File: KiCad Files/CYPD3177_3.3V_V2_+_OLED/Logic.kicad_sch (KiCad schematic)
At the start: 33 parts, among them J5 0.91 OLED, J6 QWIIC, J7 Conn_01x05, J8 I2C_3.3V, Q1 DMC2990UDJ-7, SW1 GT-TC0060-H050-L1, SW2 B3U-1000P, U1 TCA9406DC, U2 INA238, U9 ATtiny3217-M

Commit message: changes
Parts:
- added D6: PMEG6020ER, Diode_SMD:D_SOD-123F, symbol Diode:PMEG6020ER
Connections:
- net GND: now also D6.2 (A)
- net LOGIC_SW: now also U9.22 (PC5); no longer U9.1 (PA2)
- net PGOOD: now also U9.2 (PA3); no longer U9.22 (PC5)
- net Rail_2: now also D6.1 (K)
- net SW_LEFT: now also U9.1 (PA2); no longer U9.2 (PA3)
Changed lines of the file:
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@@
 	)
 	(junction
+		(at 78.74 179.07)
+		(diameter 0)
+		(color 0 0 0 0)
+	)
+	(junction
+		(at 78.74 185.42)
+		(diameter 0)
+		(color 0 0 0 0)
+	)
+	(junction
 		(at 158.75 87.63)
 		(diameter 0)
@@
 	(wire
 		(pts
+			(xy 78.74 185.42) (xy 78.74 187.96)
+		)
+		(stroke
+			(width 0)
+			(type default)
+		)
+	)
+	(wire
+		(pts
 			(xy 78.74 168.91) (xy 82.55 168.91)
 		)
@@
 	(wire
 		(pts
+			(xy 156.21 93.98) (xy 156.21 92.71)
+		)
+		(stroke
+			(width 0)
+			(type default)
+		)
+	)
+	(wire
+		(pts
 			(xy 175.26 110.49) (xy 156.21 110.49)
 		)
@@
 	(wire
 		(pts
+			(xy 82.55 185.42) (xy 78.74 185.42)
+		)
+		(stroke
+			(width 0)
+			(type default)
+		)
+	)
+	(wire
+		(pts
+			(xy 78.74 179.07) (xy 78.74 185.42)
+		)
+		(stroke
+			(width 0)
+			(type default)
+		)
+	)
+	(wire
+		(pts
 			(xy 78.74 179.07) (xy 82.55 179.07)
 		)
@@
 			"AAAAAAAAAAAAAAAAAAAAAAAAAAAAAAAAAAAAAAAAAAAAAAAAAAAAAAAAAAAAAAAAAAAAAAAAAAAA"
 			"AAAAAAAAAAAAAAAAAAAAAAAAAAAAAAAAAAAAAAAAAAAAAAAAAAAAAAAAAAAAAAAAAAAAAAAAAAAA"
+			"AAAAAAAAAAAAAAAAAAAAAAAAAAAAAAAAAAAAAAAAAAAAAAAAAAAAAAAAAAAAAAAAAAAAAAAAAAAA"
+			"AAAAAAAAAAAAAAAAAAAAAAAAAAAAAAAAAAAAAAAAAAAAAAAAAAAAAAAAAAAAAAAAAAAAAAAAAAAA"
+			"AAAAAAAAAAAAAAAAAAAAAAAAAAAAAAAAAAAAAAAAAAAAAAAAAAAAAAAAAAAAAAAAAAAAAAAAAAAA"
+			"AAAAAAAAAAAAAAAAAAAAAAAAAAAAAAAAAAAAAAAAAAAAAAAAAAAAAAAAAAAAAAAAAAAAAAAAAAAA"
+			"AAAAAAAAAAAAAAAAAAAAAAAAAAAAAAAAAAAAAAAAAAAAAAAAAAAAAAAAAAAAAAAAAAAAAAAAAAAA"
+			"AAAAAAAAAAAAAAAAAAAAAAAAAAAAAAAAAAAAAAAAAAAAAAAAAAAAAAAAAAAAAAAAAAAAAAAAAAAA"
+			"AAAAAAAAAAAAAAAAAAAAAAAAAAAAAAAAAAAAAAAAAAAAAAAAAAAAAAAAAAAAAAAAAAAAAAAAAAAA"
+			"AAAAAAAAAAAAAAAAAAAAAAAAAAAAAAAAAAAAAAAAAAAAAAAAAAAAAAAAAAAAAAAAAAAAAAAAAAAA"
+			"AAAAAAAAAAAAAAAAAAAAAAAAAAAAAAAAAAAAAAAAAAAAAAAAAAAAAAAAAAAAAAAAAAAAAAAAAAAA"
+			"AAAAAAAAAAAAAAAAAAAAAAAAAAAAAAAAAAAAAAAAAAAAAAAAAAAAAAAAAAAAAAAAAAAAAAAAAAAA"
+			"AAAAAAAAAAAAAAAAAAAAAAAAAAAAAAAAAAAAAAAAAAAAAAAAAAAAAAAAAAAAAAAAAAAAAAAAAAAA"
+			"AAAAAAAAAAAAAAAAAAAAAAAAAAAAAAAAAAAAAAAAAAAAAAAAAAAAAAAAAAAAAAAAAAAAAAAAAAAA"
+			"AAAAAAAAAAAAAAAAAAAAAAAAAAAAAAAAAAAAAAAAAAAAAAAAAAAAAAAAAAAAAAAAAAAAAAAAAAAA"
+			"AAAAAAAAAAAAAAAAAAAAAAAAAAAAAAAAAAAAAAAAAAAAAAAAAAAAAAAAAAAAAAAAAAAAAAAAAAAA"
+			"AAAAAAAAAAAAAAAAAAAAAAAAAAAAAAAAAAAAAAAAAAAAAAAAAAAAAAAAAAAAAAAAAAAAAAAAAAAA"
+			"AAAAAAAAAAAAAAAAAAAAAAAAAAAAAAAAAAAAAAAAAAAAAAAAAAAAAAAAAAAAAAAAAAAAAAAAAAAA"
+			"AAAAAAAAAAAAAAAAAAAAAAAAAAAAAAAAAAAAAAAAAAAAAAAAAAAAAAAAAAAAAAAAAAAAAAAAAAAA"
+			"AAAAAAAAAAAAAAAAAAAAAAAAAAAAAAAAAAAAAAAAAAAAAAAAAAAAAAAAAAAAAAAAAAAAAAAAAAAA"
 			"AAAAAAAAAAAAAAAAAAAAAAAAAAAAAAAAAAAAAAAAAAAAAAAAAA=="
 		)
@@
 	)
 	(label "SW_LEFT"
-		(at 161.29 95.25 0)
+		(at 156.21 93.98 0)
 		(effects
 			(font
@@
 		)
 	)
+	(hierarchical_label "LOGIC_SW"
+		(shape input)
+		(at 125.73 123.19 180)
+		(effects
+			(font
+				(size 1.27 1.27)
+			)
+			(justify right)
+		)
+	)
 	(hierarchical_label "SDA"
 		(shape bidirectional)
@@
 	(hierarchical_label "Rail_2"
 		(shape output)
-		(at 78.74 179.07 270)
+		(at 78.74 187.96 270)
 		(effects
 			(font
@@
 	(hierarchical_label "PGOOD"
 		(shape output)
-		(at 125.73 123.19 180)
+		(at 161.29 95.25 0)
 		(effects
 			(font
 				(size 1.27 1.27)
 			)
-			(justify right)
+			(justify left)
 		)
 	)
@@
 		)
 	)
-	(hierarchical_label "LOGIC_SW"
-		(shape input)
-		(at 156.21 92.71 0)
-		(effects
-			(font
-				(size 1.27 1.27)
-			)
-			(justify left)
-		)
-	)
 	(hierarchical_label "SDA_3.3v"
 		(shape bidirectional)
@@
 	)
 	(symbol
+		(lib_id "Diode:PMEG6020ER")
+		(at 86.36 185.42 0)
+		(unit 1)
+		(exclude_from_sim no)
+		(in_bom yes)
+		(on_board yes)
+		(dnp no)
+		(property "Reference" "D6"
+			(at 83.566 192.278 90)
+			(effects
+				(font
+					(size 1.27 1.27)
+				)
+				(justify left)
+			)
+		)
+		(property "Value" "PMEG6020ER"
+			(at 90.678 196.596 90)
+			(effects
+				(font
+					(size 1.27 1.27)
+				)
+				(justify left)
+			)
+		)
+		(property "Footprint" "Diode_SMD:D_SOD-123F"
+			(at 86.36 189.865 0)
+			(effects
+				(font
+					(size 1.27 1.27)
+				)
+				(hide yes)
+			)
+		)
+		(property "Datasheet" "https://assets.nexperia.com/documents/data-sheet/PMEG6020ER.pdf"
+			(at 86.36 185.42 0)
+			(effects
+				(font
+					(size 1.27 1.27)
+				)
+				(hide yes)
+			)
+		)
+		(property "Description" "60V, 2A low Vf MEGA Schottky barrier rectifier, SOD-123W"
+			(at 86.36 185.42 0)
+			(effects
+				(font
+					(size 1.27 1.27)
+				)
+				(hide yes)
+			)
+		)
+		(pin "1"
+		)
+		(pin "2"
+		)
+		(instances
+			(project "CYPD3177_3.3V_V2_+_OLED"
+				(path "/a370047b-ebc6-4236-825e-9462ba7e4392/bd19bb82-a076-4c57-9538-864609224ca0"
+					(reference "D6")
+					(unit 1)
+				)
+			)
+		)
+	)
+	(symbol
 		(lib_id "power:GND")
 		(at 90.17 154.94 270)
@@
 					(unit 1)
 				)
+			)
+		)
+	)
+	(symbol
+		(lib_id "power:GND")
+		(at 90.17 185.42 90)
+		(unit 1)
+		(exclude_from_sim no)
+		(in_bom yes)
+		(on_board yes)
+		(dnp no)
+		(fields_autoplaced yes)
+		(property "Reference" "#PWR056"
+			(at 96.52 185.42 0)
+			(effects
+				(font
+					(size 1.27 1.27)
+				)
+				(hide yes)
+			)
+		)
+		(property "Value" "GND"
+			(at 95.25 185.42 0)
+			(effects
+				(font
+					(size 1.27 1.27)
+				)
+				(hide yes)
+			)
+		)
+		(property "Footprint" ""
+			(at 90.17 185.42 0)
+			(effects
+				(font
+					(size 1.27 1.27)
+				)
+				(hide yes)
+			)
+		)
+		(property "Datasheet" ""
+			(at 90.17 185.42 0)
+			(effects
+				(font
+					(size 1.27 1.27)
+				)
+				(hide yes)
+			)
+		)
+		(property "Description" ""
+			(at 90.17 185.42 0)
+			(effects
+				(font
+					(size 1.27 1.27)
+				)
+				(hide yes)
+			)
+		)
+		(pin "1"
+		)
+		(instances
+			(project "CYPD3177_3.3V_V2_+_OLED"
+				(path "/a370047b-ebc6-4236-825e-9462ba7e4392/bd19bb82-a076-4c57-9538-864609224ca0"
+					(reference "#PWR056")
+					(unit 1)
+				)

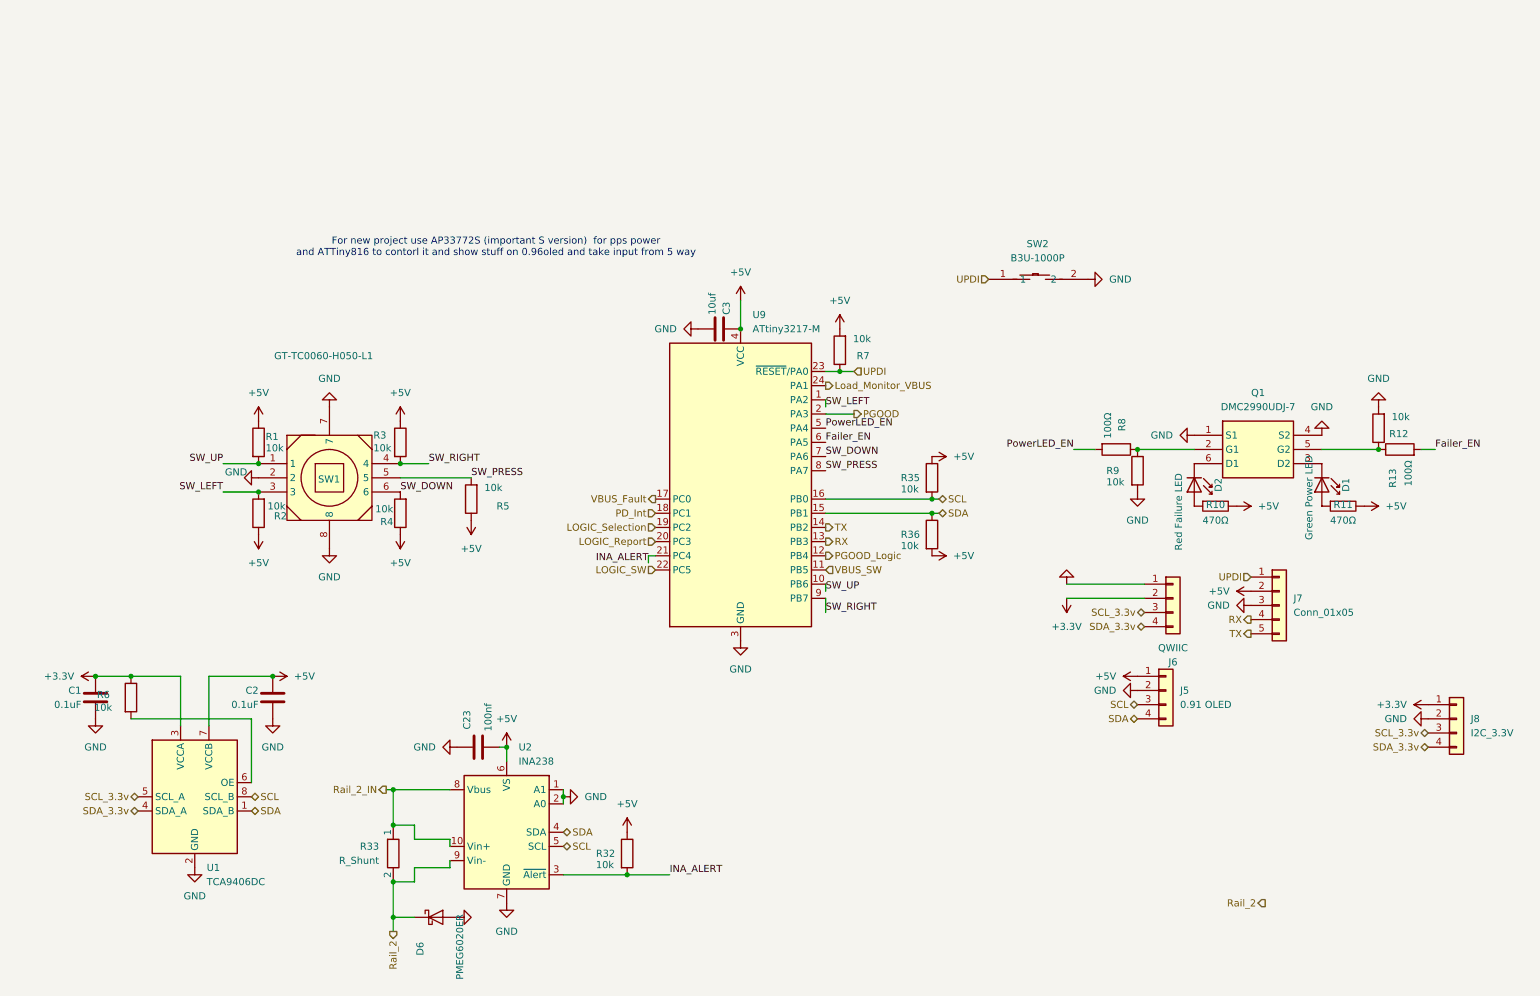
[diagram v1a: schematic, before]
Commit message: CYPD3177 wiring finshed, only silkscreen needs changes and make a breakout board
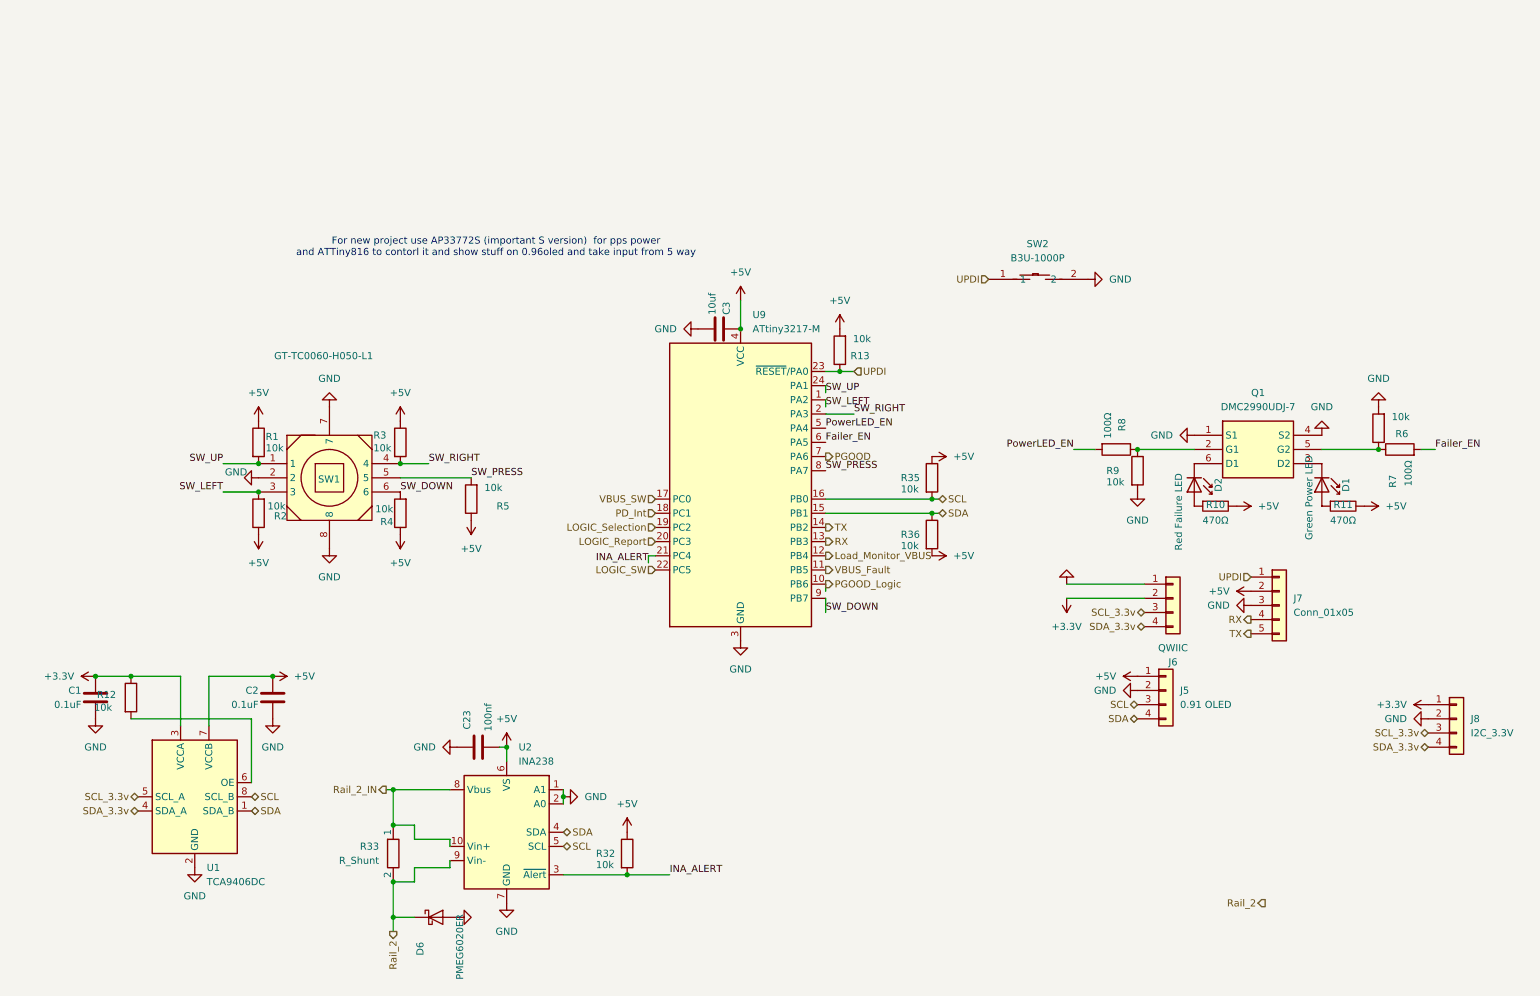
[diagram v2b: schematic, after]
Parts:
- R10, R11: footprint Resistor_SMD:R_0402_1005Metric_Pad0.72x0.64mm_HandSolder -> Resistor_SMD:R_0402_1005Metric
- renumbered R6 to R12, R7 to R13, R12 to R6, R13 to R7
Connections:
- net Load_Monitor_VBUS: now also U9.12 (PB4); no longer U9.24 (PA1)
- net PGOOD: now also U9.7 (PA6); no longer U9.2 (PA3)
- net PGOOD_Logic: now also U9.10 (PB6); no longer U9.12 (PB4)
- net SW_DOWN: now also U9.9 (PB7); no longer U9.7 (PA6)
- net SW_RIGHT: now also U9.2 (PA3); no longer U9.9 (PB7)
- net SW_UP: now also U9.24 (PA1); no longer U9.10 (PB6)
- net VBUS_Fault: now also U9.11 (PB5); no longer U9.17 (PC0)
- net VBUS_SW: now also U9.17 (PC0); no longer U9.11 (PB5)
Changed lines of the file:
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@@
 	(wire
 		(pts
+			(xy 156.21 91.44) (xy 156.21 90.17)
+		)
+		(stroke
+			(width 0)
+			(type default)
+		)
+	)
+	(wire
+		(pts
 			(xy 156.21 127) (xy 156.21 125.73)
 		)
@@
 			"AAAAAAAAAAAAAAAAAAAAAAAAAAAAAAAAAAAAAAAAAAAAAAAAAAAAAAAAAAAAAAAAAAAAAAAAAAAA"
 			"AAAAAAAAAAAAAAAAAAAAAAAAAAAAAAAAAAAAAAAAAAAAAAAAAAAAAAAAAAAAAAAAAAAAAAAAAAAA"
-			"AAAAAAAAAAAAAAAAAAAAAAAAAAAAAAAAAAAAAAAAAAAAAAAAAA=="
-		)
-	)
-	(label "SW_DOWN"
-		(at 156.21 102.87 0)
-		(effects
-			(font
-				(size 1.27 1.27)
-			)
-			(justify left bottom)
+			"AAAAAAAAAAAAAAAAAAAAAAAAAAAAAAAAAAAAAAAAAAAAAAAAAAAAAAAAAAAAAAAAAAAAAAAAAAAA"
+			"AAAAAAAAAAAAAAAAAAAAAAAAAAAAAAAAAAAAAAAAAAAAAAAAAAAAAAAAAAAAAAAAAAAAAAAAAAAA"
+			"AAAAAAAAAAAAAAAAAAAAAAAAAAAAAAAAAAAAAAAAAAAAAAAAAAAAAAAAAAAAAAAAAAAAAAAAAAAA"
+			"AAAAAAAAAAAAAAAAAAAAAAAAAAAAAAAAAAAAAAAAAAAAAAAAAAAAAAAAAAAAAAAAAAAAAAAAAAAA"
+			"AAAAAAAAAAAAAAAAAAAAAAAAAAAAAAAAAAAAAAAAAAAAAAAAAAAAAAAAAAAAAAAAAAAAAAAAAAAA"
+			"AAAAAAAAAAAAAAAAAAAAAAAAAAAAAAAAAAAAAAAAAAAAAAAAAAAAAAAAAAAAAAAAAAAAAAAAAAAA"
+			"AAAAAAAAAAAAAAAAAAAAAAAAAAAAAAAAAAAAAAAAAAAAAAAAAAAAAAAAAAAAAAAAAAAAAAAAAAAA"
+			"AAAAAAAAAAAAAAAAAAAAAAAAAAAAAAAAAAAAAAAAAAAAAAAAAAAAAAAAAAAAAAAAAAAAAAAAAAAA"
+			"AAAAAAAAAAAAAAAAAAAAAAAAAAAAAAAAAAAAAAAAAAAAAAAAAAAAAAAAAAAAAAAAAAAAAAAAAAAA"
+			"AAAAAAAAAAAAAAAAAAAAAAAAAAAAAAAAAAAAAAAAAAAAAAAAAAAAAAAAAAAAAAAAAAAAAAAAAAAA"
+			"AAAAAAAAAAAAAAAAAAAAAAAAAAAAAAAAAAAAAAAAAAAAAAAAAAAAAAAAAAAAAAAAAAAAAAAAAAAA"
+			"AAAAAAAAAAAAAAAAAAAAAAAAAAAAAAAAAAAAAAAAAAAAAAAAAAAAAAAAAAAAAAAAAAAAAAAAAAAA"
+			"AAAAAAAAAAAAAAAAAAAAAAAAAAAAAAAAAAAAAAAAAAAAAAAAAAAAAAAAAAAAAAAAAAAAAAAAAAAA"
+			"AAAAAAAAAAAAAAAAAAAAAAAAAAAAAAAAAAAAAAAAAAAAAAAAAAAAAAAAAAAAAAAAAAAAAAAAAAAA"
+			"AAAAAAAAAAAAAAAAAAAAAAAAAAAAAAAAAAAAAAAAAAAAAAAAAAAAAAAAAAAAAAAAAAAAAAAAAAAA"
+			"AAAAAAAAAAAAAAAAAAAAAAAAAAAAAAAAAAAAAAAAAAAAAAAAAAAAAAAAAAAAAAAAAAAAAAAAAAAA"
+			"AAAAAAAAAAAAAAAAAAAAAAAAAAAAAAAAAAAAAAAAAAAAAAAAAAAAAAAAAAAAAAAAAAAAAAAAAAAA"
+			"AAAAAAAAAAAAAAAAAAAAAAAAAAAAAAAAAAAAAAAAAAAAAAAAAAAAAAAAAAAAAAAAAAAAAAAAAAAA"
+			"AAAAAAAAAAAAAAAAAAAAAAAAAAAAAAAAAAAAAAAAAAAAAAAAAGkAYQBuAGcALAAgAEYAWABMADEA"
+			"MAA1ADAALAAgADEAMAAuADkANQB4ADEAMAAuADAAeAA0AC4AOABtAG0ALAAgACgAaAB0AHQAcABz"
+			"ADoALwAvAHcAdwB3AC4AbABjAHMAYwAuAGMAbwBtAC8AZABhAHQAYQBzAGgAZQBlAHQALwBsAGMA"
+			"cwBjAF8AZABhAHQAYQBzAGgAZQBlAHQAXwAyADQAMAA0ADIANgAwADkAMgAxAF8AYwBqAGkAYQBu"
+			"AGcALQAtAEMAaABhAG4AZwBqAGkAYQBuAGcALQBNAGkAYwByAG8AZQBsAGUAYwB0AHIAbwBuAGkA"
+			"YwBzAC0AVABlAGMAaAAtAEYAWABMADAANAAyADAALQAyAFIAMgAtAE0AXwBDADEANgA3ADIAMAA2"
+			"AC4AcABkAGYAKQAsACAAZwBlAG4AZQByAGEAdABlAGQAIAB3AGkAdABoACAAawBpAGMAYQBkAC0A"
+			"ZgBvAG8AdABwAHIAaQBuAHQALQBnAGUAbgBlAHIAYQB0AG8AcgAgAGcAZQBuAF8AaQBuAGQAdQBj"
+			"AHQAbwByAC4AcAB5AAAAaGFuZ2VkLCBpZD1zZWxmLkdldElkKNlOn04gEACASQBuAGQAdQBjAHQA"
+			"bwByACwAIABDAGgAYQBuAGcAagBpAGEAbgBnACwAIABGAFgATAAxADAANQAwACwAIAAxADAALgA5"
+			"ADUAeAAxADAALgAwAHgANAAuADgAbQBtACwAIAAoAGgAdAB0AHAAcwA6AC8ALwB3AHcAdwAuAGwA"
+			"YwBzAGMALgBjAG8AbQAvAGQAYQB0AGEAcwBoAGUAZQB0AC8AbABjAHMAYwBfAGQAYQB0AGEAcwBo"
+			"AGUAZQB0AF8AMgA0ADAANAAyADYAMAA5ADIAMQBfAGMAagBpAGEAbgBnAC0ALQBDAGgAYQBuAGcA"
+			"agBpAGEAbgBnAC0ATQBpAGMAcgBvAGUAbABlAGMAdAByAG8AbgBpAGMAcwAtAFQAZQBjAGgALQBG"
+			"AFgATAAwADQAMgAwAC0AMgBSADIALQBNAF8AQwAxADYANwAyADAANgAuAHAAZABmACkALAAgAGcA"
+			"ZQBuAGUAcgBhAHQAZQBkACAAdwBpAHQAaAAgAGsAaQBjAGEAZAAtAGYAbwBvAHQAcAByAGkAbgB0"
+			"AC0AZwBlAG4AZQByAGEAdABvAHIAIABnAGUAbgBfAGkAbgBkAHUAYwB0AG8AcgAuAHAAeQAAAHdp"
+			"bmRvdyA9IHNlbGYuR2V0UGFnZSg4T3hNYxEAgEkAbgBkAHUAYwB0AG8AcgAsACAAQwBoAGEAbgBn"
+			"AGoAaQBhAG4AZwAsACAARgBYAEwAMgAyADEAMwAsACAAMgAyAA=="
 		)
 	)
@@
 		)
 	)
-	(label "SW_RIGHT"
-		(at 156.21 130.81 0)
+	(label "Failer_EN"
+		(at 156.21 100.33 0)
 		(effects
 			(font
@@
 		)
 	)
-	(label "Failer_EN"
-		(at 156.21 100.33 0)
+	(label "SW_UP"
+		(at 156.21 91.44 0)
+		(effects
+			(font
+				(size 1.27 1.27)
+			)
+			(justify left bottom)
+		)
+	)
+	(label "SW_DOWN"
+		(at 156.21 130.81 0)
 		(effects
 			(font
@@
 		)
 	)
-	(label "INA_ALERT"
-		(at 124.46 121.92 180)
+	(label "SW_RIGHT"
+		(at 161.29 95.25 0)
 		(effects
 			(font
 				(size 1.27 1.27)
 			)
-			(justify right bottom)
+			(justify left bottom)
 		)
 	)
-	(label "SW_UP"
-		(at 48.26 104.14 180)
+	(label "INA_ALERT"
+		(at 124.46 121.92 180)
 		(effects
 			(font
@@
 	)
 	(label "SW_UP"
-		(at 156.21 127 0)
+		(at 48.26 104.14 180)
 		(effects
 			(font
 				(size 1.27 1.27)
 			)
-			(justify left bottom)
+			(justify right bottom)
 		)
 	)
@@
 		)
 	)
-	(hierarchical_label "PGOOD_Logic"
-		(shape output)
-		(at 156.21 120.65 0)
-		(effects
-			(font
-				(size 1.27 1.27)
-			)
-			(justify left)
-		)
-	)
 	(hierarchical_label "LOGIC_SW"
 		(shape input)
@@
 		)
 	)
+	(hierarchical_label "PGOOD_Logic"
+		(shape output)
+		(at 156.21 125.73 0)
+		(effects
+			(font
+				(size 1.27 1.27)
+			)
+			(justify left)
+		)
+	)
 	(hierarchical_label "SDA"
 		(shape bidirectional)
@@
 		)
 	)
+	(hierarchical_label "PGOOD"
+		(shape output)
+		(at 156.21 102.87 0)
+		(effects
+			(font
+				(size 1.27 1.27)
+			)
+			(justify left)
+		)
+	)
 	(hierarchical_label "TX"
 		(shape output)
@@
 	(hierarchical_label "VBUS_SW"
 		(shape input)
-		(at 156.21 123.19 0)
+		(at 125.73 110.49 180)
 		(effects
 			(font
 				(size 1.27 1.27)
 			)
-			(justify left)
+			(justify right)
 		)
 	)
@@
 	(hierarchical_label "Load_Monitor_VBUS"
 		(shape output)
-		(at 156.21 90.17 0)
+		(at 156.21 120.65 0)
 		(effects
 			(font
@@
 		)
 	)
-	(hierarchical_label "VBUS_Fault"
-		(shape output)
-		(at 125.73 110.49 180)
+	(hierarchical_label "SCL_3.3v"
+		(shape bidirectional)
+		(at 33.02 163.83 180)
 		(effects
 			(font
@@
 		)
 	)
-	(hierarchical_label "SCL_3.3v"
-		(shape bidirectional)
-		(at 33.02 163.83 180)
+	(hierarchical_label "VBUS_Fault"
+		(shape output)
+		(at 156.21 123.19 0)
 		(effects
 			(font
 				(size 1.27 1.27)
 			)
-			(justify right)
+			(justify left)
 		)
 	)
@@
 		)
 	)
-	(hierarchical_label "PGOOD"
-		(shape output)
-		(at 161.29 95.25 0)
-		(effects
-			(font
-				(size 1.27 1.27)
-			)
-			(justify left)
-		)
-	)
 	(hierarchical_label "TX"
 		(shape output)
@@
 			)
 		)
-		(property "Footprint" "Resistor_SMD:R_0402_1005Metric_Pad0.72x0.64mm_HandSolder"
+		(property "Footprint" "Resistor_SMD:R_0402_1005Metric"
 			(at 226.949 116.078 0)
 			(effects
@@
 		(on_board yes)
 		(dnp no)
-		(property "Reference" "R6"
+		(property "Reference" "R12"
 			(at 25.654 145.542 0)
 			(effects
@@
 			(project "CYPD3177_3.3V_V2_+_OLED"
 				(path "/a370047b-ebc6-4236-825e-9462ba7e4392/bd19bb82-a076-4c57-9538-864609224ca0"
-					(reference "R6")
+					(reference "R12")
 					(unit 1)
 				)
@@
 		(on_board yes)
 		(dnp no)
-		(property "Reference" "R13"
+		(property "Reference" "R7"
 			(at 257.81 108.458 0)
 			(effects
@@
 			(project "CYPD3177_3.3V_V2_+_OLED"
 				(path "/a370047b-ebc6-4236-825e-9462ba7e4392/bd19bb82-a076-4c57-9538-864609224ca0"
-					(reference "R13")
+					(reference "R7")
 					(unit 1)
 				)
@@
 		(on_board yes)
 		(dnp no)
-		(property "Reference" "R7"
+		(property "Reference" "R13"
 			(at 164.084 84.836 0)
 			(effects
@@
 			(project "CYPD3177_3.3V_V2_+_OLED"
 				(path "/a370047b-ebc6-4236-825e-9462ba7e4392/bd19bb82-a076-4c57-9538-864609224ca0"
-					(reference "R7")
+					(reference "R13")
 					(unit 1)
 				)
@@
 		(on_board yes)
 		(dnp no)
-		(property "Reference" "R12"
+		(property "Reference" "R6"
 			(at 260.604 98.806 0)
 			(effects
@@
 			(project "CYPD3177_3.3V_V2_+_OLED"
 				(path "/a370047b-ebc6-4236-825e-9462ba7e4392/bd19bb82-a076-4c57-9538-864609224ca0"
-					(reference "R12")
+					(reference "R6")
 					(unit 1)
 				)
@@
 			)
 		)
-		(property "Footprint" "Resistor_SMD:R_0402_1005Metric_Pad0.72x0.64mm_HandSolder"
+		(property "Footprint" "Resistor_SMD:R_0402_1005Metric"
 			(at 249.809 116.078 0)
 			(effects
